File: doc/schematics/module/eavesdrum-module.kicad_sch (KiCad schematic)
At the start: 98 parts, among them J1 DC37_Pins_MountingHoles, J2 Conn_02x25_Odd_Even, J3 Conn_01x03, J4 Conn_01x20_Pin, J5 Conn_01x20_Pin, SW1 SW_Push, SW2 SW_Push, SW3 SW_Push, U1 CD74HC4067M, U2 CD74HC4067M

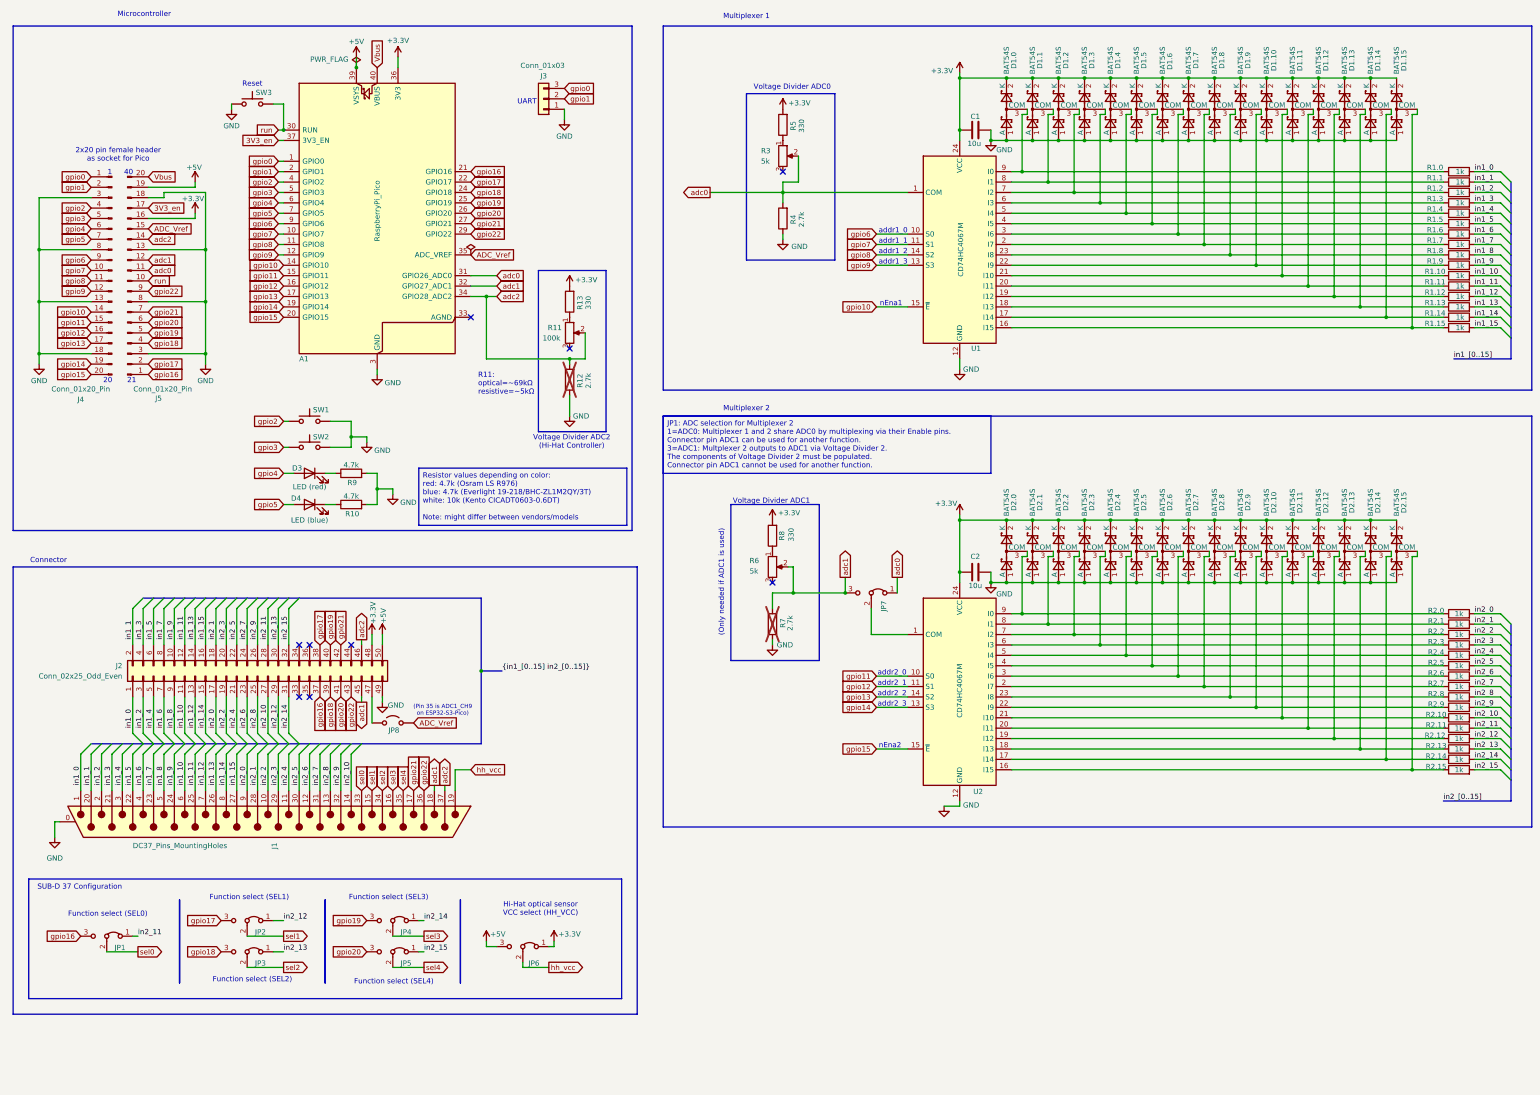
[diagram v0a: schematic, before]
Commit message: schematics for module 1.2
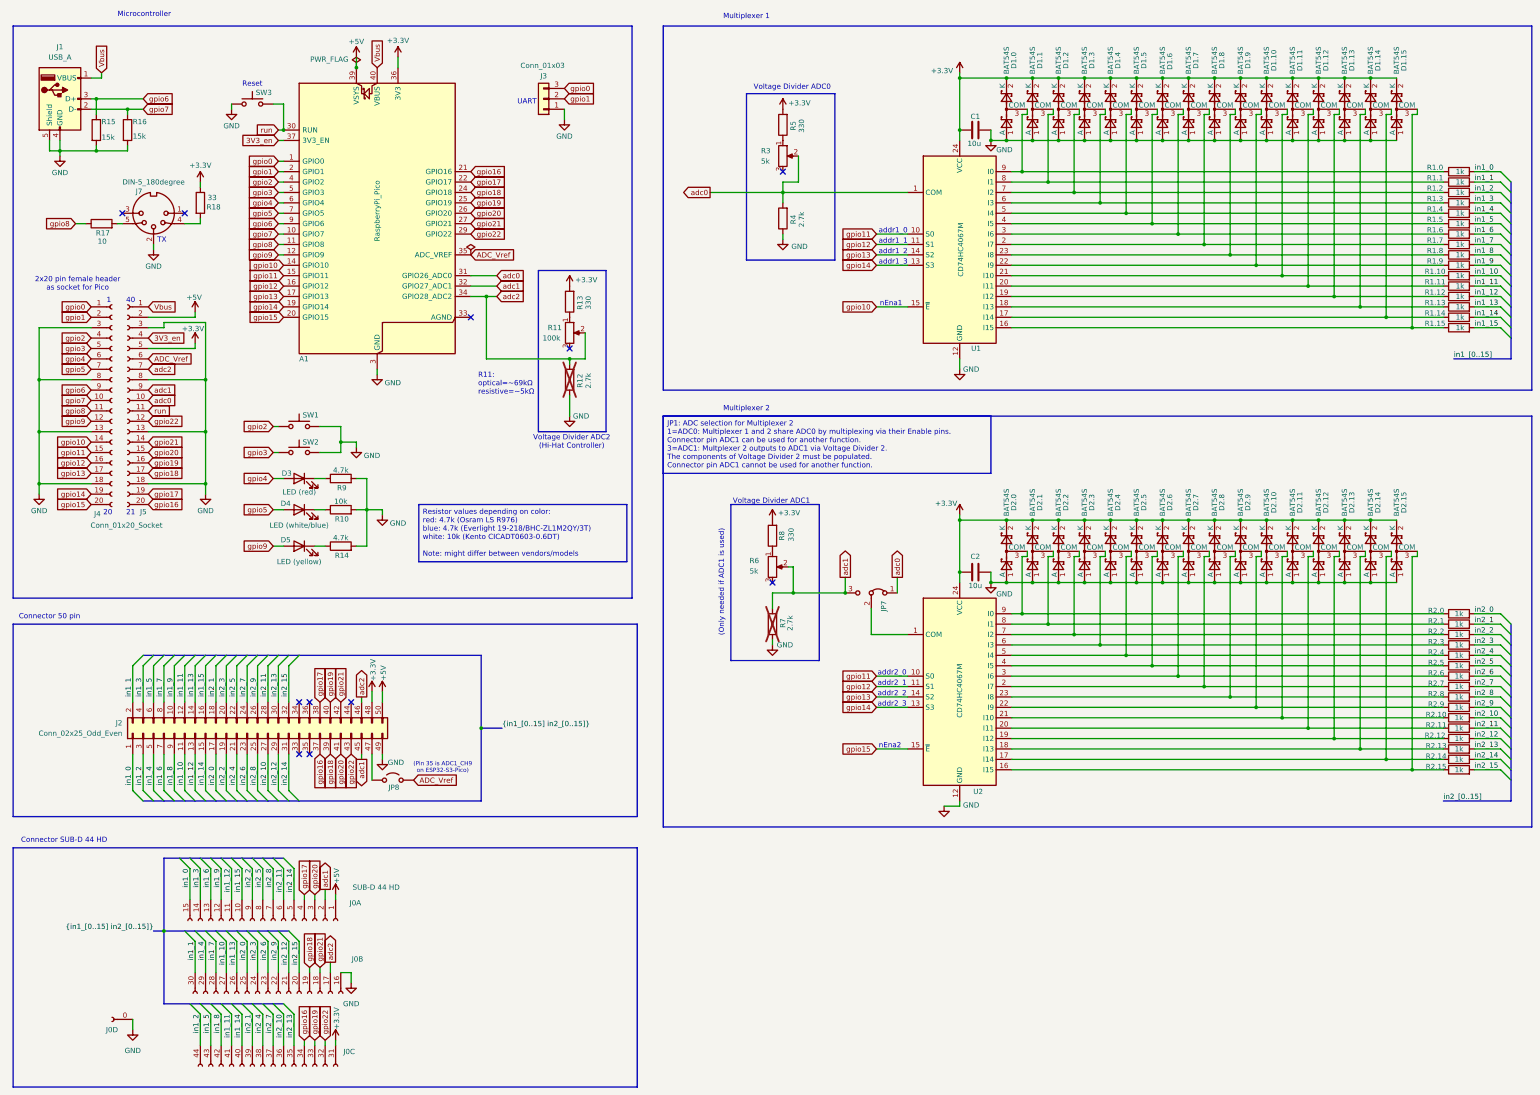
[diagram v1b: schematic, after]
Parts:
- removed J1: DC37_Pins_MountingHoles, Connector_Dsub:DSUB-37_Pins_Horizontal_P2.77x2.84mm_EdgePinOffset7.70mm_Housed_MountingHolesOffset9.12mm, symbol Connector:DC37_Pins_MountingHoles
- removed JP1, JP2, JP3, JP4, JP5, JP6: Jumper, Connector_PinHeader_2.54mm:PinHeader_1x03_P2.54mm_Vertical_SMD_Pin1Right, symbol Jumper:Jumper_3_Bridged12
- added D5: LED (yellow), EavesDrum:LED_D3.0mm_SMD_Thru, symbol Device:LED
- added J0: SUB-D 44 HD, Connector_Dsub:DSUB-44-HD_Socket_Horizontal_P2.29x2.54mm_EdgePinOffset8.35mm_Housed_MountingHolesOffset10.89mm, symbol Conn_01x44_Socket_3_rows_sym:Conn_01x44_Socket_3_rows
- added J1: USB_A, Connector_USB:USB_A_Connfly_DS1095, symbol Connector:USB_A
- added J7: DIN-5_180degree, EavesDrum:MIDI_DIN5, symbol Connector:DIN-5_180degree
- added R14: 4.7k, Resistor_SMD:R_0805_2012Metric, symbol Device:R
- added R15, R16: 15k, Resistor_SMD:R_0805_2012Metric, symbol Device:R
- added R17: 10, Resistor_SMD:R_0805_2012Metric, symbol Device:R
- added R18: 33, Resistor_SMD:R_0805_2012Metric, symbol Device:R
- D3: footprint LED_THT:LED_D3.0mm -> EavesDrum:LED_D3.0mm_SMD_Thru
- D4: value LED (blue) -> LED (white/blue); footprint LED_THT:LED_D3.0mm -> EavesDrum:LED_D3.0mm_SMD_Thru
- J2: footprint Connector_IDC:IDC-Header_2x25_P2.54mm_Vertical -> EavesDrum:IDC-Header_2x25_P2.54mm_Vertical_SMD_Thru
- J3: footprint Connector_PinSocket_2.54mm:PinSocket_1x03_P2.54mm_Vertical_SMD_Pin1Left -> EavesDrum:PinSocket_1x03_P2.54mm_Vertical_SMD_Thru_Pin1Left
- J4: value Conn_01x20_Pin -> Conn_01x20_Socket; footprint Connector_PinSocket_2.54mm:PinSocket_1x20_P2.54mm_Vertical -> EavesDrum:RaspberryPi_Pico_wo_2nd_pin_row; symbol Connector:Conn_01x20_Pin -> Connector:Conn_01x20_Socket
- J5: value Conn_01x20_Pin -> Conn_01x20_Socket; footprint Connector_PinSocket_2.54mm:PinSocket_1x20_P2.54mm_Vertical -> EavesDrum:RaspberryPi_Pico_Common_2nd_pin_row; symbol Connector:Conn_01x20_Pin -> Connector:Conn_01x20_Socket
- R10: value 4.7k -> 10k
- R11, R3, R6: footprint Potentiometer_SMD:Potentiometer_ACP_CA9-VSMD_Vertical -> EavesDrum:Potentiometer_SMD_Thru_Vertical
- SW1, SW2, SW3: footprint Button_Switch_SMD:SW_Push_1P1T_NO_CK_KSC6xxJ -> EavesDrum:SW_Push_SMD_Thru
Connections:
- net +3.3V: now also J5.5 (Pin_5), J0.31 (Pin_31), R18.1; no longer J5.16 (Pin_16)
- net +5V: now also J5.2 (Pin_2), J0.1 (Pin_1); no longer J5.19 (Pin_19)
- net 3V3_en: now also J5.4 (Pin_4); no longer J5.17 (Pin_17)
- net ADC_Vref: now also J5.6 (Pin_6); no longer J5.15 (Pin_15)
- net GND: now also J0.0 (Pin_44), J0.16 (Pin_16), J1.4 (GND), J1.5 (Shield), J7.2, R14.2, R15.2, R16.2
- net Vbus: now also J5.1 (Pin_1), J1.1 (VBUS); no longer J5.20 (Pin_20)
- net adc0: now also J5.10 (Pin_10); no longer J5.11 (Pin_11)
- net adc1: now also J5.9 (Pin_9), J0.2 (Pin_2); no longer J5.12 (Pin_12)
- net adc2: now also J5.7 (Pin_7), J0.17 (Pin_17); no longer J5.14 (Pin_14)
- net gpio11: now also U1.10 (S0)
- net gpio12: now also U1.11 (S1)
- net gpio13: now also U1.14 (S2)
- net gpio14: now also U1.13 (S3)
- net gpio16: now also J5.20 (Pin_20), J0.34 (Pin_34); no longer J5.1 (Pin_1)
- net gpio17: now also J5.19 (Pin_19), J0.4 (Pin_4); no longer J5.2 (Pin_2)
- net gpio18: now also J5.17 (Pin_17), J0.19 (Pin_19); no longer J5.4 (Pin_4)
- net gpio19: now also J5.16 (Pin_16), J0.33 (Pin_33); no longer J5.5 (Pin_5)
- net gpio20: now also J5.15 (Pin_15), J0.3 (Pin_3); no longer J5.6 (Pin_6)
- net gpio21: now also J5.14 (Pin_14), J0.18 (Pin_18); no longer J5.7 (Pin_7)
- net gpio22: now also J5.12 (Pin_12), J0.32 (Pin_32); no longer J5.9 (Pin_9)
- net gpio6: now also J1.3 (D+), R15.1; no longer U1.10 (S0)
- net gpio7: now also J1.2 (D-), R16.1; no longer U1.11 (S1)
- net gpio8: now also R17.1; no longer U1.14 (S2)
- net gpio9: now also D5.2 (A); no longer U1.13 (S3)
- net in1_0: now also J0.15 (Pin_15)
- net in1_1: now also J0.30 (Pin_30)
- net in1_10: now also J0.27 (Pin_27)
- net in1_11: now also J0.41 (Pin_41)
- net in1_12: now also J0.11 (Pin_11)
- net in1_13: now also J0.26 (Pin_26)
- net in1_14: now also J0.40 (Pin_40)
- net in1_15: now also J0.10 (Pin_10)
- net in1_2: now also J0.44 (Pin_44)
- net in1_3: now also J0.14 (Pin_14)
- net in1_4: now also J0.29 (Pin_29)
- net in1_5: now also J0.43 (Pin_43)
- net in1_6: now also J0.13 (Pin_13)
- net in1_7: now also J0.28 (Pin_28)
- net in1_8: now also J0.42 (Pin_42)
- net in1_9: now also J0.12 (Pin_12)
- net in2_0: now also J0.25 (Pin_25)
- net in2_1: now also J0.39 (Pin_39)
- net in2_10: now also J0.36 (Pin_36)
- net in2_11: now also J0.6 (Pin_6)
- net in2_12: now also J0.21 (Pin_21)
- net in2_13: now also J0.35 (Pin_35)
- net in2_14: now also J0.5 (Pin_5)
- net in2_15: now also J0.20 (Pin_20)
- net in2_2: now also J0.9 (Pin_9)
- net in2_3: now also J0.24 (Pin_24)
- net in2_4: now also J0.38 (Pin_38)
- net in2_5: now also J0.8 (Pin_8)
- net in2_6: now also J0.23 (Pin_23)
- net in2_7: now also J0.37 (Pin_37)
- net in2_8: now also J0.7 (Pin_7)
- net in2_9: now also J0.22 (Pin_22)
- net run: now also J5.11 (Pin_11); no longer J5.10 (Pin_10)
- new net: D5.1 (K), R14.1
- new net: J7.5, R17.2
- new net: J7.4, R18.2
- no-connect marks 9 -> 11
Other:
- note added: "Connector 50 pin"
- note added: "Connector SUB-D 44 HD"
- note added: "TX"
- note removed: "Connector"
- note removed: "Function select (SEL0)"
- note removed: "Function select (SEL1)"
- note removed: "Function select (SEL2)"
- note removed: "Function select (SEL3)"
- note removed: "Function select (SEL4)"
- note removed: "Hi-Hat optical sensor VCC select (HH_VCC)"
- note removed: "SUB-D 37 Configuration"
- moved on the sheet: D3, D4, J2, JP8, R10, R9, SW1, SW2
